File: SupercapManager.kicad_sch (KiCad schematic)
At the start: 7 parts, among them J1 JST4_M, J2 XT30_M, J3 XT30_M, J4 XT30_M, J5 XT30_M, Q5 BSC015NE2LS5I, Q8 BSC015NE2LS5I

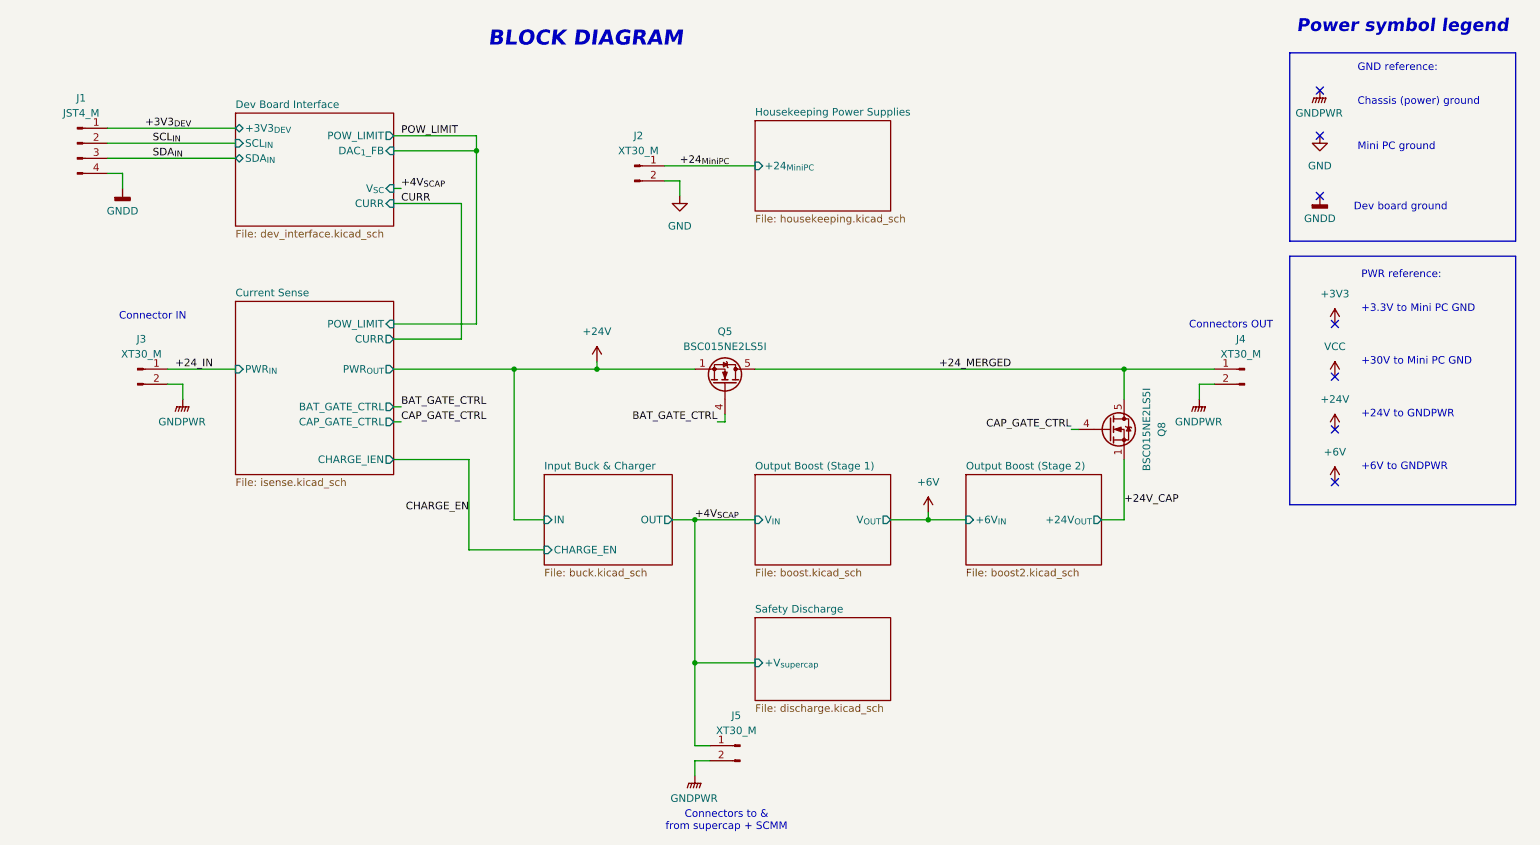
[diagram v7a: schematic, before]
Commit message: Tuned circuits & adjusted values
Changed footprints for some circuits to consolidate components
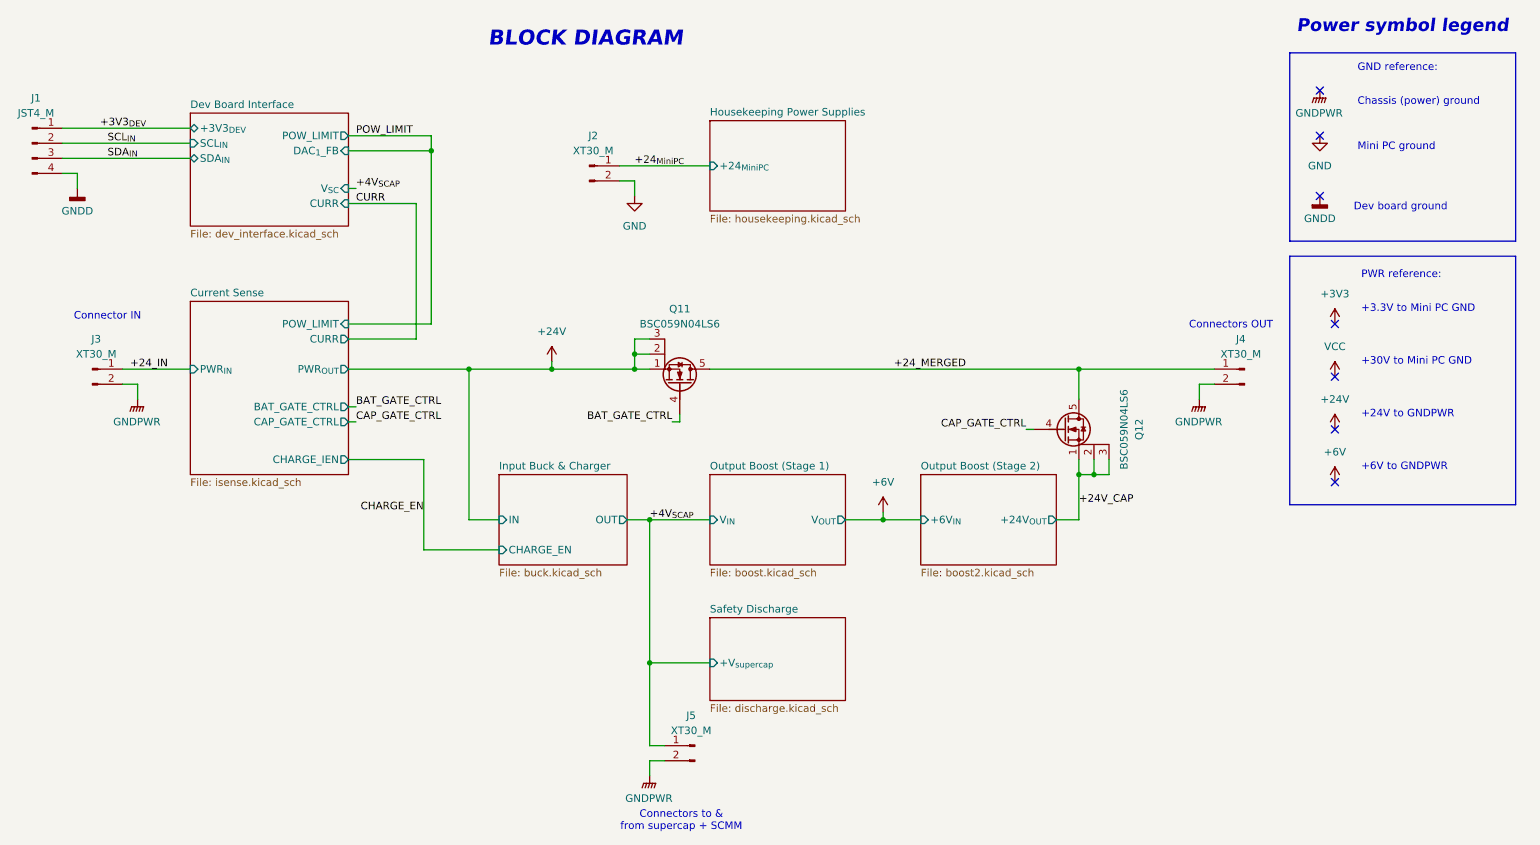
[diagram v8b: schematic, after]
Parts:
- removed Q5, Q8: BSC015NE2LS5I, Package_TO_SOT_SMD:TDSON-8-1, symbol Transistor_FET:BSC026N08NS5
- added Q11, Q12: BSC059N04LS6, Package_SON:Infineon_PG-TDSON-8_6.15x5.15mm, symbol Transistor_FET:Q_NMOS_SGD
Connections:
- net +24V: now also Q11.1 (S), Q11.2 (S), Q11.3 (S)
- net +24V_CAP: now also Q12.1 (S), Q12.2 (S), Q12.3 (S)
- net +24_MERGED: now also Q11.5 (D), Q12.5 (D)
- net BAT_GATE_CTRL: now also Q11.4 (G)
- net CAP_GATE_CTRL: now also Q12.4 (G)
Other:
- moved on the sheet: J1, J2, J3, J5
